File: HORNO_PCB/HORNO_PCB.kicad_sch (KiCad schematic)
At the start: 100 parts, among them J0_1 Alimentacion dispositivo seri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, J0_10 Terminales de tornillo espaci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, J0_11 Terminales de tornillo espaci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, J0_12 Terminales de tornillo espaci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, J0_13 Terminales de tornillo espaci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, J0_14 Terminales de tornillo espaci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, J0_15 Terminales de tornillo espaci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, J0_16 Terminales de tornillo espaci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, J0_17 Terminales de tornillo espaci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, J0_18 Terminales de tornillo espaci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, J0_19 Terminales de tornillo espaci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, J0_2 Terminales de tornillo espaci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, J0_3 Terminales de tornillo espaci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, J0_4 Terminales de tornillo espaci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, J0_5 Terminales de tornillo espaci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, J0_6 Terminales de tornillo espaci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, J0_7 Terminales de tornillo espaci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, J0_8 Terminales de tornillo espaci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, J0_9 Terminales de tornillo espaci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, J1 +5V +24V, J24 Screw_Terminal_01x20, J25 Screw_Terminal_01x20, J26 Screw_Terminal_01x20, J27 Screw_Terminal_01x20, J7 24VDC, K1 Relay 1, K2 Relay 2, K7 Relay 3, K8 Relay 2, K9 Relay 1, Q1 2N2222, Q2 2N2222, Q6 IRG4PF50W, Q7 IRG4PF50W, U1 TLP521-1, U10 LM741, U15 TLP250, U17 LM741, U18 LM741, U19 TLP250, U2 TLP521-1, U25 UDN2981A, U3 TLP521-1, U4 TLP521-1, U9 LM741

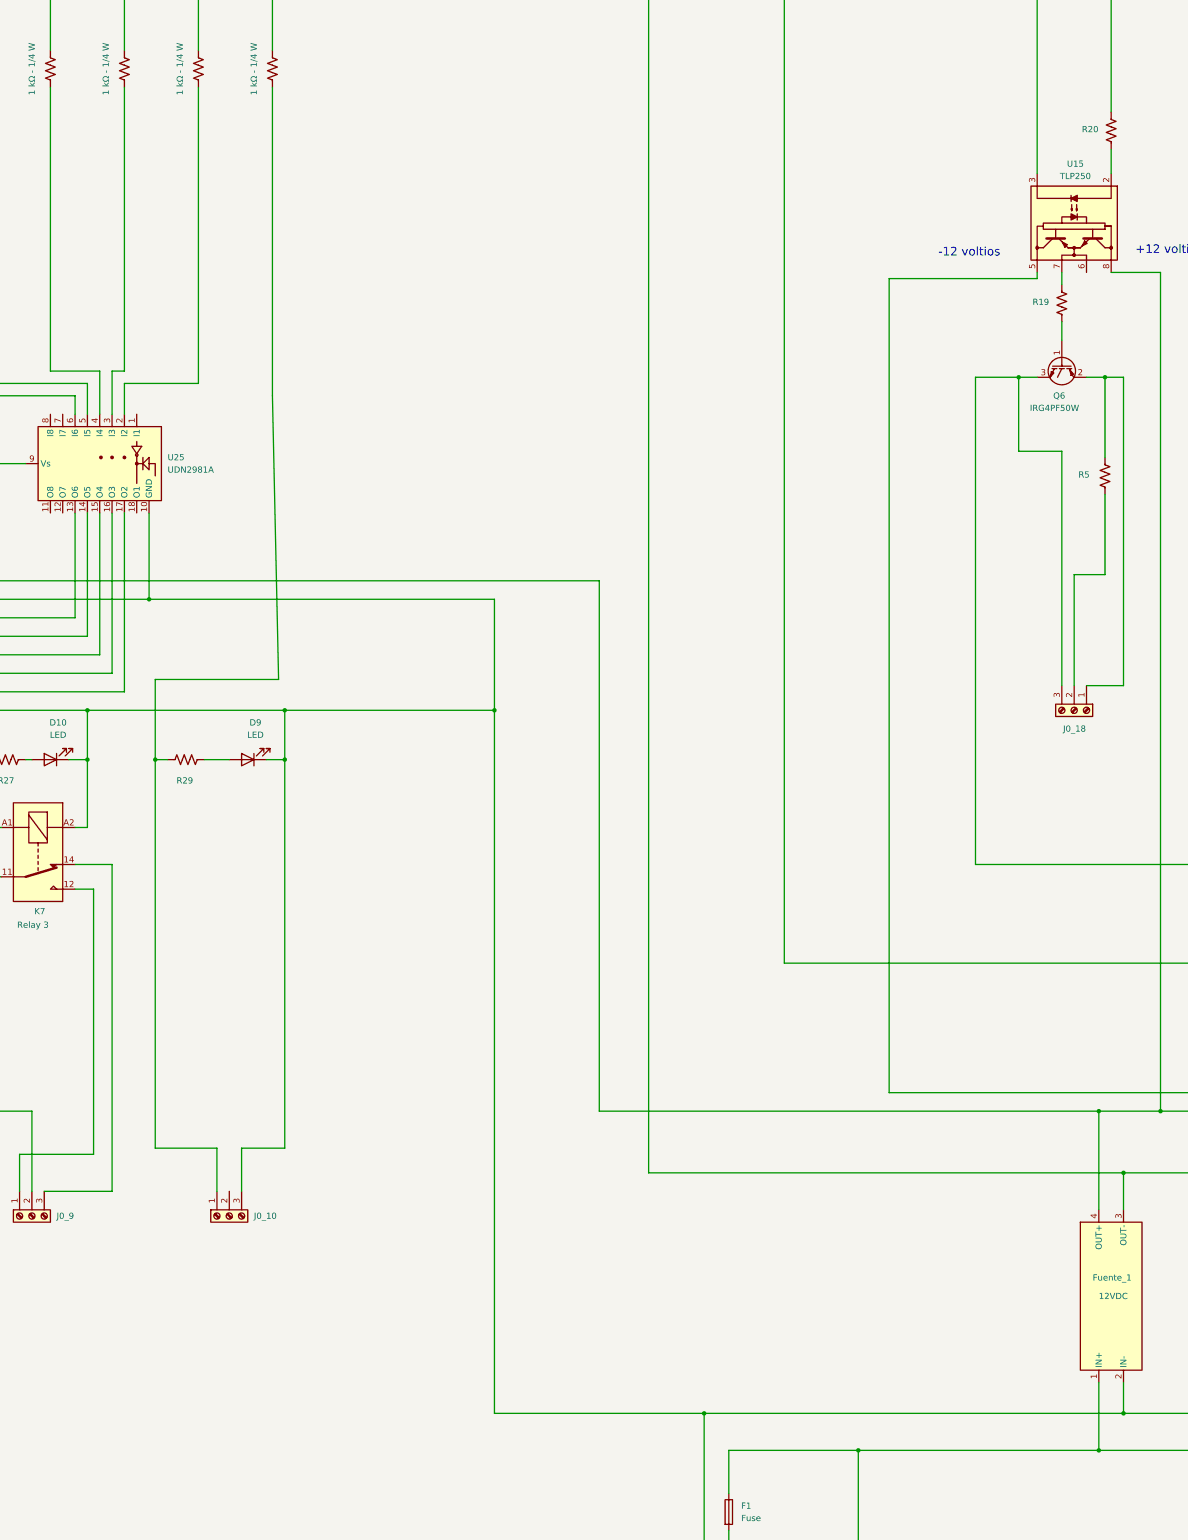
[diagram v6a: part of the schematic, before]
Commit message: Alimentacion de 24V para el UDN y cambiar rele de salida para conectar un SSR
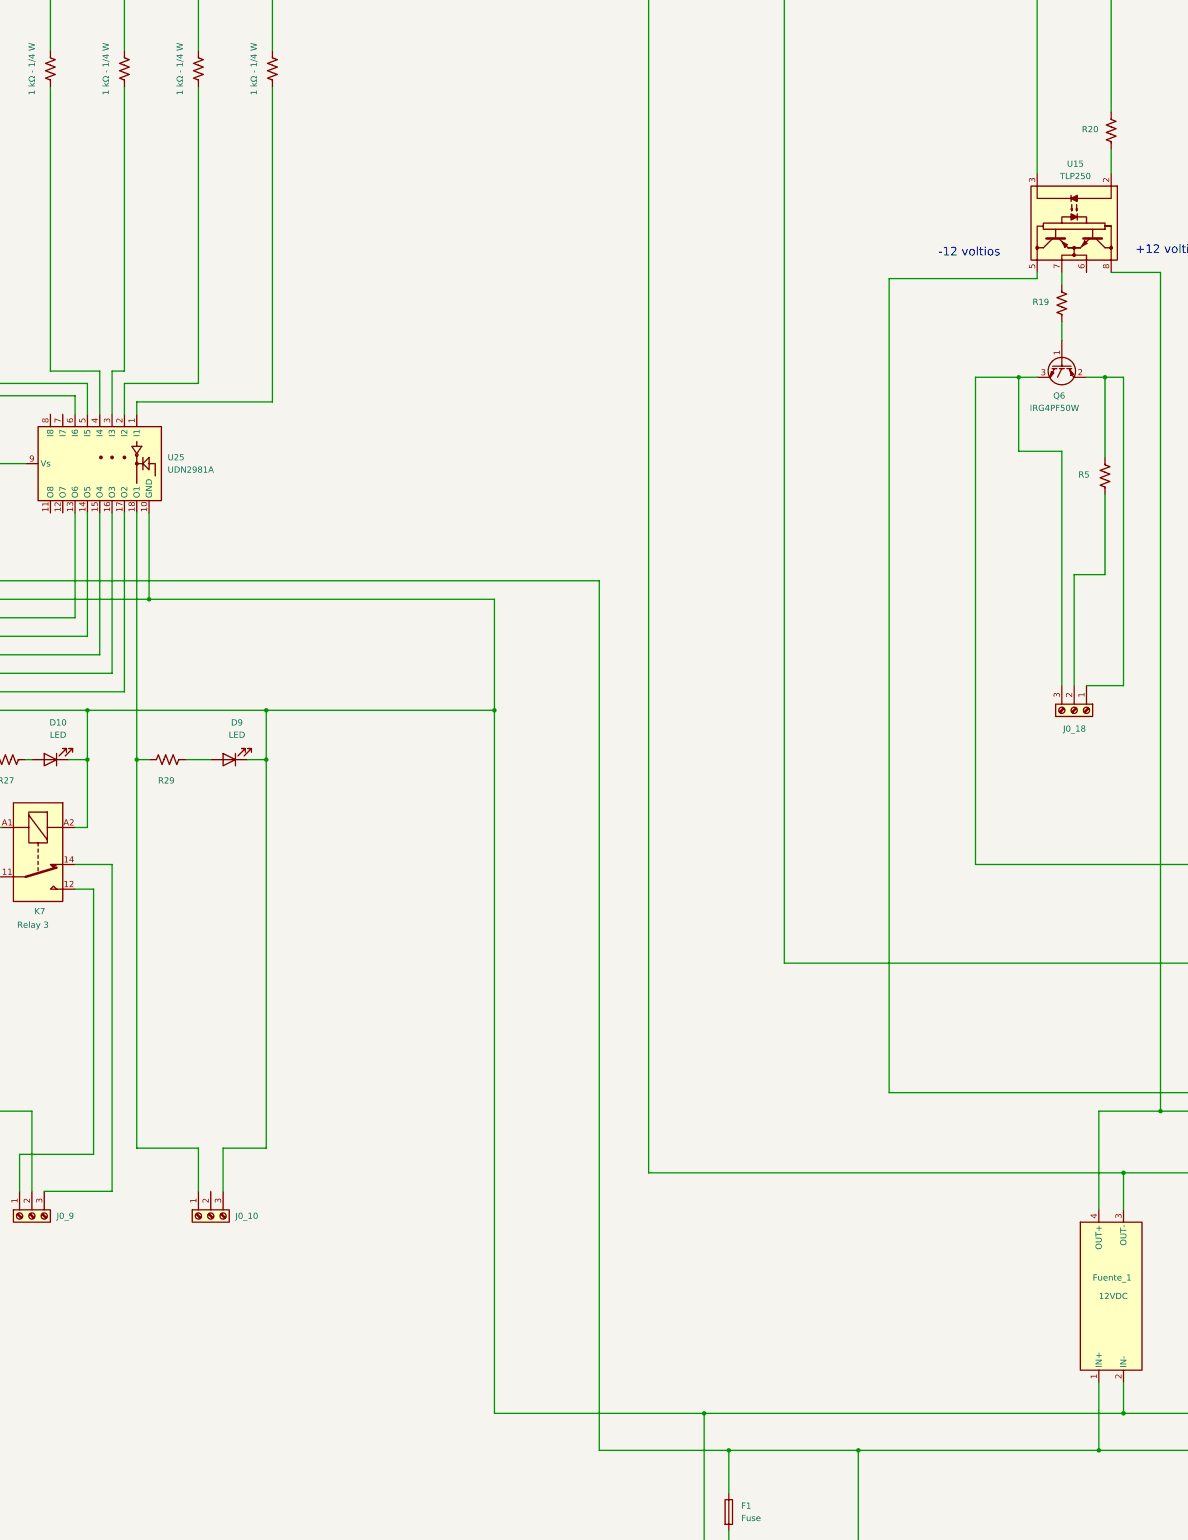
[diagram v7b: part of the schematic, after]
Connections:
- net at Fuente_1.4 (OUT+), U10.7 (V+), U15.8 (VCC)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: no longer U25.9 (Vs)
- net at F1.1, Fuente_1.1 (IN+), Fuente_2.1 (IN+)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: now also U25.9 (Vs)
- net at J0_10.1 (Pin_1), R29.2: now also U25.18 (O1); no longer R48.1
- net at U25.1 (I1): now also R48.1
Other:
- moved on the sheet: D9, J0_10, R29
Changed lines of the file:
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@@
 	)
 	(junction
-		(at 681.99 613.41)
-		(diameter 0)
-		(color 0 0 0 0)
-	)
-	(junction
 		(at 341.63 530.86)
 		(diameter 0)
@@
 	)
 	(junction
+		(at 605.79 683.26)
+		(diameter 0)
+		(color 0 0 0 0)
+	)
+	(junction
 		(at 163.83 284.48)
 		(diameter 0)
@@
 	)
 	(junction
-		(at 514.35 541.02)
+		(at 510.54 541.02)
 		(diameter 0)
 		(color 0 0 0 0)
@@
 	)
 	(junction
-		(at 514.35 530.86)
+		(at 510.54 530.86)
 		(diameter 0)
 		(color 0 0 0 0)
@@
 	)
 	(junction
-		(at 487.68 541.02)
+		(at 483.87 541.02)
 		(diameter 0)
 		(color 0 0 0 0)
@@
 	(wire
 		(pts
-			(xy 487.68 524.51) (xy 487.68 541.02)
-		)
-		(stroke
-			(width 0)
-			(type default)
-		)
-	)
-	(wire
-		(pts
 			(xy 323.85 565.15) (xy 318.77 565.15)
 		)
@@
 	(wire
 		(pts
-			(xy 510.54 541.02) (xy 514.35 541.02)
+			(xy 506.73 541.02) (xy 510.54 541.02)
 		)
 		(stroke
@@
 	(wire
 		(pts
-			(xy 579.12 613.41) (xy 681.99 613.41)
-		)
-		(stroke
-			(width 0)
-			(type default)
-			(color 255 11 0 1)
-		)
-	)
-	(wire
-		(pts
 			(xy 812.8 570.23) (xy 812.8 577.85)
 		)
@@
 	(wire
 		(pts
+			(xy 473.71 530.86) (xy 510.54 530.86)
+		)
+		(stroke
+			(width 0)
+			(type default)
+			(color 0 0 0 1)
+		)
+	)
+	(wire
+		(pts
 			(xy 191.77 314.96) (xy 195.58 314.96)
 		)
@@
 	(wire
 		(pts
-			(xy 514.35 541.02) (xy 514.35 621.03)
+			(xy 510.54 541.02) (xy 510.54 621.03)
 		)
 		(stroke
@@
 	(wire
 		(pts
-			(xy 497.84 541.02) (xy 502.92 541.02)
+			(xy 494.03 541.02) (xy 499.11 541.02)
 		)
 		(stroke
@@
 	(wire
 		(pts
-			(xy 473.71 530.86) (xy 514.35 530.86)
-		)
-		(stroke
-			(width 0)
-			(type default)
-			(color 0 0 0 1)
-		)
-	)
-	(wire
-		(pts
 			(xy 407.67 541.02) (xy 410.21 541.02)
 		)
@@
 	(wire
 		(pts
-			(xy 487.68 541.02) (xy 487.68 621.03)
+			(xy 483.87 541.02) (xy 483.87 621.03)
 		)
 		(stroke
@@
 	(wire
 		(pts
-			(xy 500.38 621.03) (xy 500.38 629.92)
+			(xy 496.57 621.03) (xy 496.57 629.92)
 		)
 		(stroke
@@
 	(wire
 		(pts
-			(xy 579.12 504.19) (xy 579.12 613.41)
+			(xy 579.12 504.19) (xy 579.12 683.26)
 		)
 		(stroke
@@
 	(wire
 		(pts
+			(xy 579.12 683.26) (xy 605.79 683.26)
+		)
+		(stroke
+			(width 0)
+			(type default)
+			(color 255 11 0 1)
+		)
+	)
+	(wire
+		(pts
 			(xy 76.2 353.06) (xy 95.25 353.06)
 		)
@@
 	(wire
 		(pts
-			(xy 514.35 530.86) (xy 514.35 541.02)
+			(xy 510.54 530.86) (xy 510.54 541.02)
 		)
 		(stroke
@@
 	(wire
 		(pts
-			(xy 513.08 524.51) (xy 487.68 524.51)
+			(xy 483.87 490.22) (xy 483.87 541.02)
 		)
 		(stroke
@@
 	(wire
 		(pts
-			(xy 511.81 402.59) (xy 511.81 466.09)
-		)
-		(stroke
-			(width 0)
-			(type default)
-		)
-	)
-	(wire
-		(pts
 			(xy 331.47 629.92) (xy 331.47 613.41)
 		)
@@
 	(wire
 		(pts
-			(xy 514.35 621.03) (xy 505.46 621.03)
+			(xy 510.54 621.03) (xy 501.65 621.03)
 		)
 		(stroke
@@
 	(wire
 		(pts
-			(xy 514.35 530.86) (xy 557.53 530.86)
+			(xy 510.54 530.86) (xy 557.53 530.86)
 		)
 		(stroke
@@
 	(wire
 		(pts
+			(xy 511.81 402.59) (xy 511.81 467.36)
+		)
+		(stroke
+			(width 0)
+			(type default)
+		)
+	)
+	(wire
+		(pts
 			(xy 1029.97 347.98) (xy 1068.07 347.98)
 		)
@@
 	(wire
 		(pts
-			(xy 487.68 621.03) (xy 500.38 621.03)
+			(xy 483.87 621.03) (xy 496.57 621.03)
 		)
 		(stroke
@@
 	(wire
 		(pts
+			(xy 511.81 467.36) (xy 483.87 467.36)
+		)
+		(stroke
+			(width 0)
+			(type default)
+		)
+	)
+	(wire
+		(pts
 			(xy 417.83 541.02) (xy 420.37 541.02)
 		)
@@
 	(wire
 		(pts
-			(xy 505.46 621.03) (xy 505.46 629.92)
+			(xy 501.65 621.03) (xy 501.65 629.92)
 		)
 		(stroke
@@
 	(wire
 		(pts
-			(xy 490.22 541.02) (xy 487.68 541.02)
+			(xy 486.41 541.02) (xy 483.87 541.02)
 		)
 		(stroke
@@
 	(wire
 		(pts
+			(xy 483.87 467.36) (xy 483.87 469.9)
+		)
+		(stroke
+			(width 0)
+			(type default)
+		)
+	)
+	(wire
+		(pts
 			(xy 450.85 541.02) (xy 450.85 554.99)
 		)
@@
 	(wire
 		(pts
-			(xy 511.81 466.09) (xy 513.08 524.51)
-		)
-		(stroke
-			(width 0)
-			(type default)
-		)
-	)
-	(wire
-		(pts
 			(xy 133.35 353.06) (xy 133.35 772.16)
 		)
@@
 	(symbol
 		(lib_id "Connector:Screw_Terminal_01x03")
-		(at 502.92 635 90)
+		(at 499.11 635 90)
 		(unit 1)
 		(exclude_from_sim no)
@@
 		(fields_autoplaced yes)
 		(property "Reference" "J0_10"
-			(at 508 634.9999 90)
+			(at 504.19 634.9999 90)
 			(effects
 				(font
@@
 		)
 		(property "Value" "Terminales de tornillo espaciados en 5mm"
-			(at 504.1899 637.54 0)
+			(at 500.3799 637.54 0)
 			(effects
 				(font
@@
 		)
 		(property "Footprint" "TerminalBlock_Phoenix:TerminalBlock_Phoenix_PT-1,5-3-5.0-H_1x03_P5.00mm_Horizontal"
-			(at 502.92 635 0)
+			(at 499.11 635 0)
 			(effects
 				(font
@@
 		)
 		(property "Datasheet" "~"
-			(at 502.92 635 0)
+			(at 499.11 635 0)
 			(effects
 				(font
@@
 		)
 		(property "Description" "Terminales de tornillo espaciados en 3.5mm"
-			(at 502.92 635 0)
+			(at 499.11 635 0)
 			(effects
 				(font
@@
 	(symbol
 		(lib_id "Device:R_US")
-		(at 494.03 541.02 270)
+		(at 490.22 541.02 270)
 		(unit 1)
 		(exclude_from_sim no)
@@
 		(dnp no)
 		(property "Reference" "R29"
-			(at 493.776 545.338 90)
+			(at 489.966 545.338 90)
 			(effects
 				(font
@@
 		)
 		(property "Value" "Depende de la aplicación salida analógica"
-			(at 494.03 544.83 90)
+			(at 490.22 544.83 90)
 			(effects
 				(font
@@
 		)
 		(property "Footprint" "Resistor_THT:R_Axial_DIN0207_L6.3mm_D2.5mm_P10.16mm_Horizontal"
-			(at 493.776 542.036 90)
+			(at 489.966 542.036 90)
 			(effects
 				(font
@@
 		)
 		(property "Datasheet" "~"
-			(at 494.03 541.02 0)
+			(at 490.22 541.02 0)
 			(effects
 				(font
@@
 		)
 		(property "Description" "Resistor, US symbol"
-			(at 494.03 541.02 0)
+			(at 490.22 541.02 0)
 			(effects
 				(font
@@
 	(symbol
 		(lib_id "Device:LED")
-		(at 506.73 541.02 180)
+		(at 502.92 541.02 180)
 		(unit 1)
 		(exclude_from_sim no)
@@
 		(fields_autoplaced yes)
 		(property "Reference" "D9"
-			(at 508.3175 533.4 0)
+			(at 504.5075 533.4 0)
 			(effects
 				(font
@@
 		)
 		(property "Value" "LED"
-			(at 508.3175 535.94 0)
+			(at 504.5075 535.94 0)
 			(effects
 				(font
@@
 		)
 		(property "Footprint" "LED_THT:LED_D4.0mm"
-			(at 506.73 541.02 0)
+			(at 502.92 541.02 0)
 			(effects
 				(font
@@
 		)
 		(property "Datasheet" "~"
-			(at 506.73 541.02 0)
+			(at 502.92 541.02 0)
 			(effects
 				(font
@@
 		)
 		(property "Description" "Light emitting diode"
-			(at 506.73 541.02 0)
+			(at 502.92 541.02 0)
 			(effects
 				(font
@@
 		)
 		(property "Sim.Pins" "1=K 2=A"
-			(at 506.73 541.02 0)
+			(at 502.92 541.02 0)
 			(effects
 				(font
